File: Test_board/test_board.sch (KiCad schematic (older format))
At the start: 29 parts, among them J1 CONN_01X03_MALE, J2 CONN_02X20, J3 CONN_01X06, J4 CONN_02X20, J5 USB_A, J8 DB9_FEMALE, U1 MAX16056

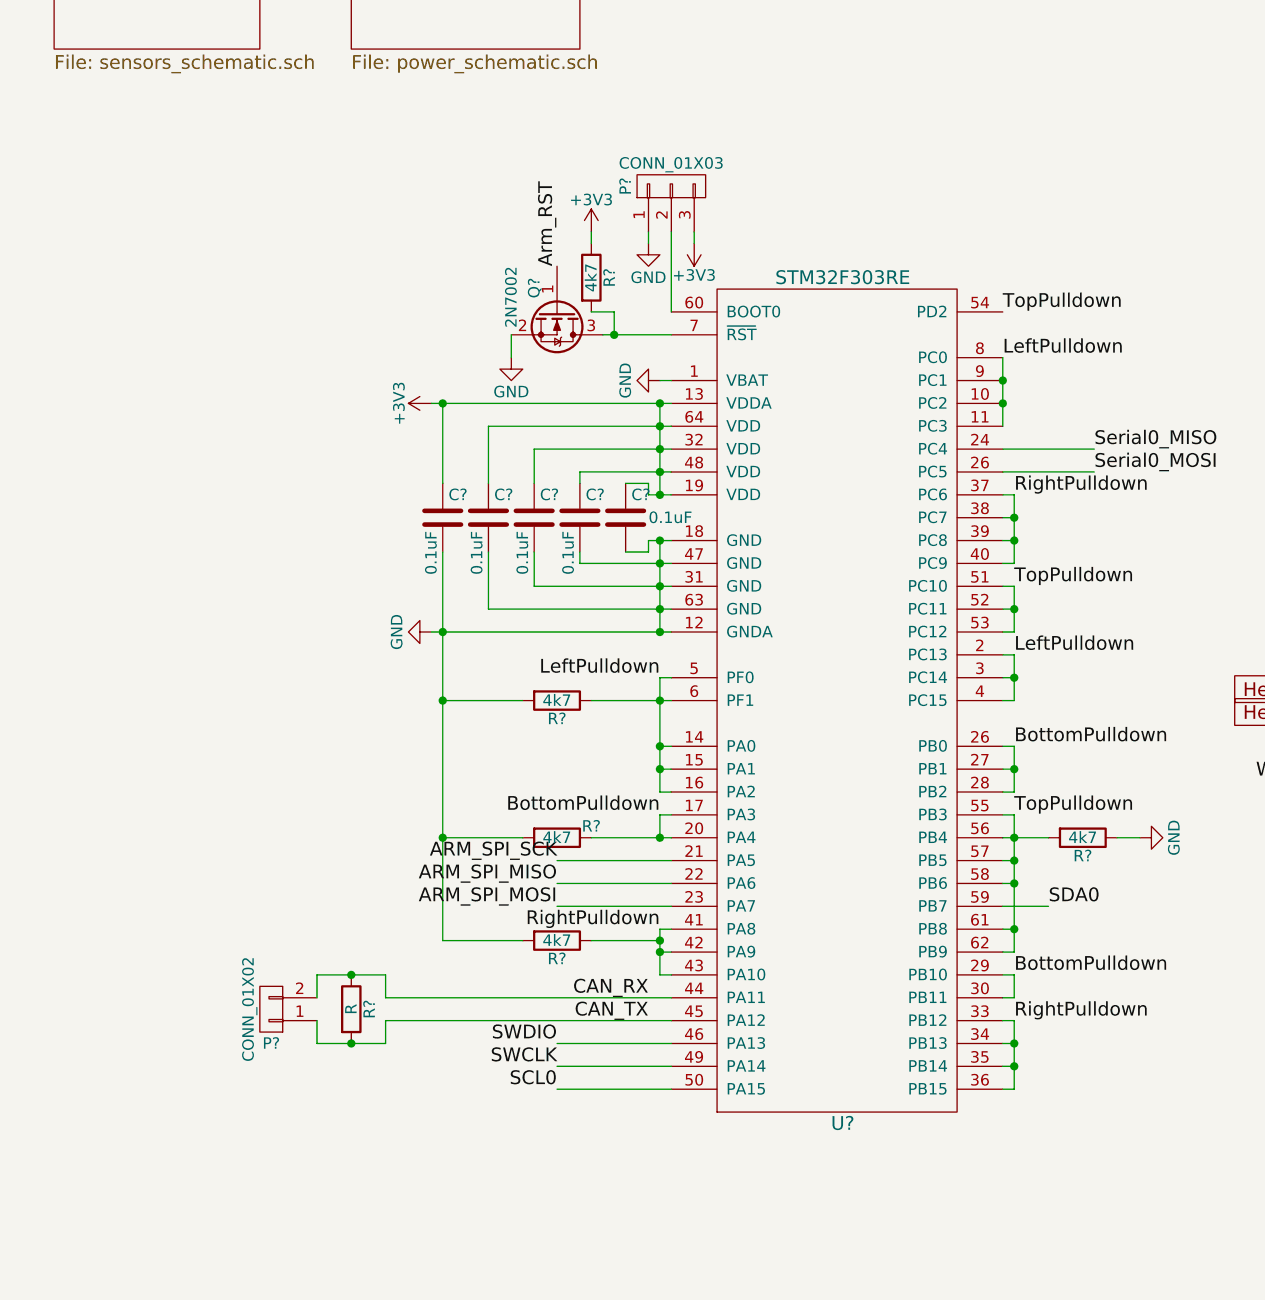
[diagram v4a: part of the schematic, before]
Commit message: Added programming header to diagram. Changed drafting template
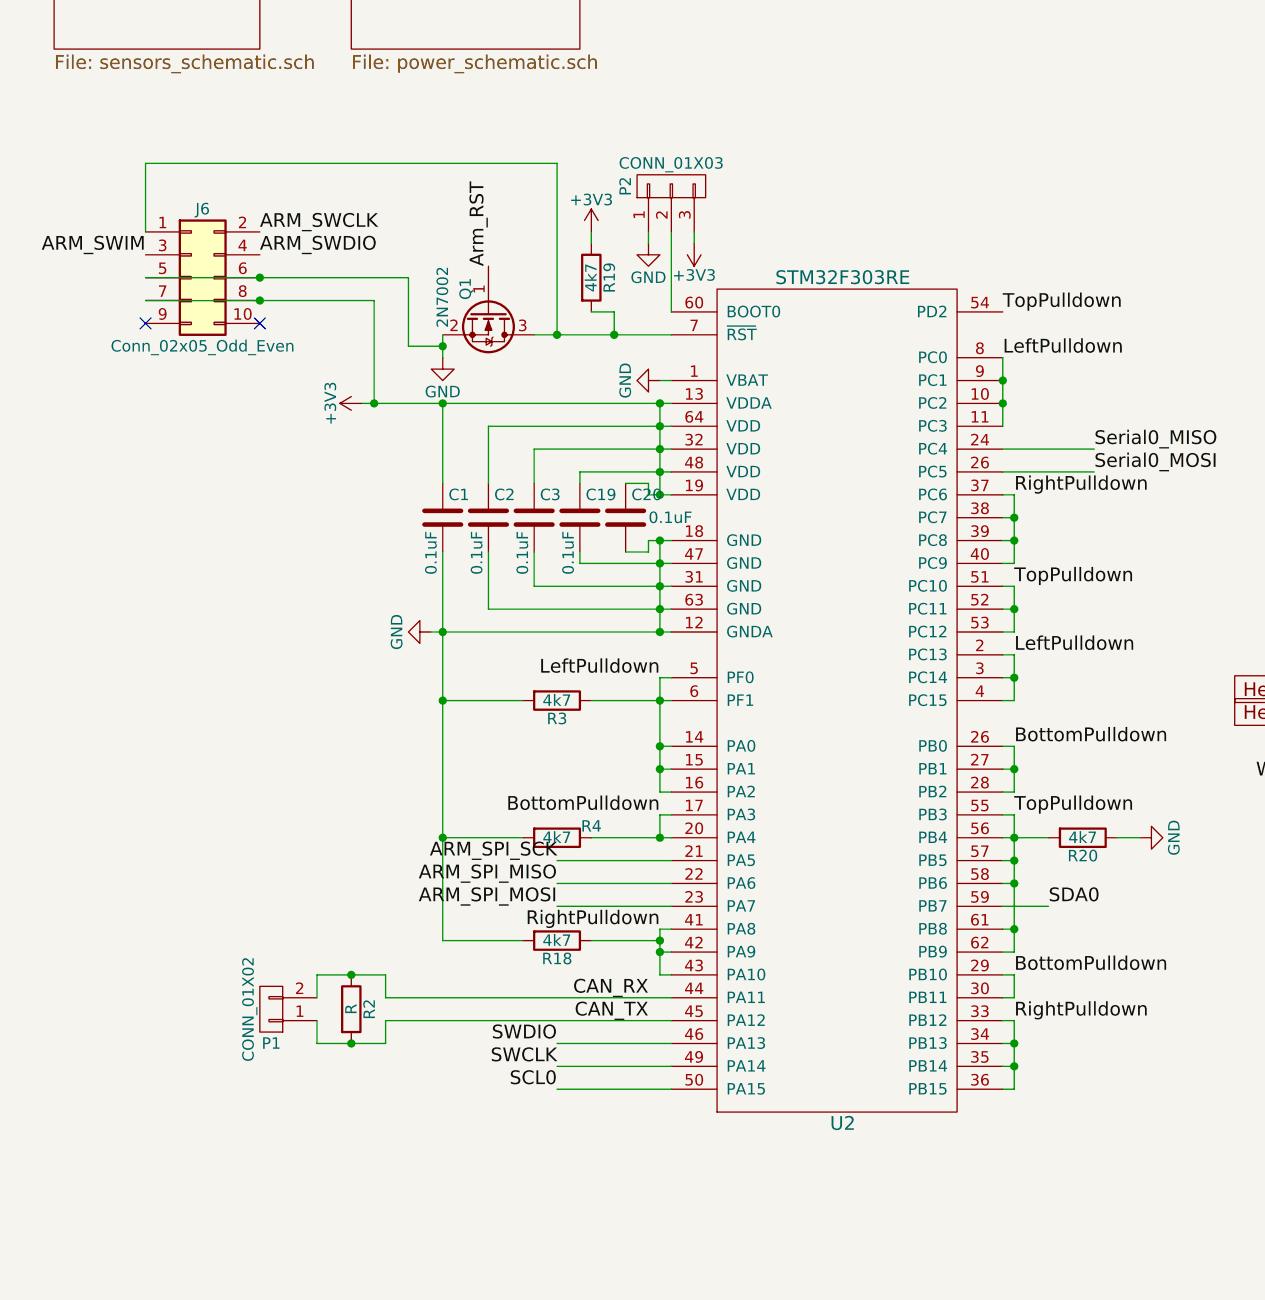
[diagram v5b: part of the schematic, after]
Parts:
- added J6: Conn_02x05_Odd_Even, symbol Conn_02x05_Odd_Even
- gave numbers to parts that had none: 15
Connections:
- net +3V3: now also J6.7 (Pin_7), J6.8 (Pin_8)
- net GND: now also J6.5 (Pin_5), J6.6 (Pin_6)
- net at Q1.3 (D), R19.2, U2.7 (~RST): now also J6.1 (Pin_1)
- new net ARM_SWCLK: J6.2 (Pin_2)
- new net ARM_SWDIO: J6.4 (Pin_4)
- new net ARM_SWIM: J6.3 (Pin_3)
- no-connect marks 7 -> 9
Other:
- moved on the sheet: Q1

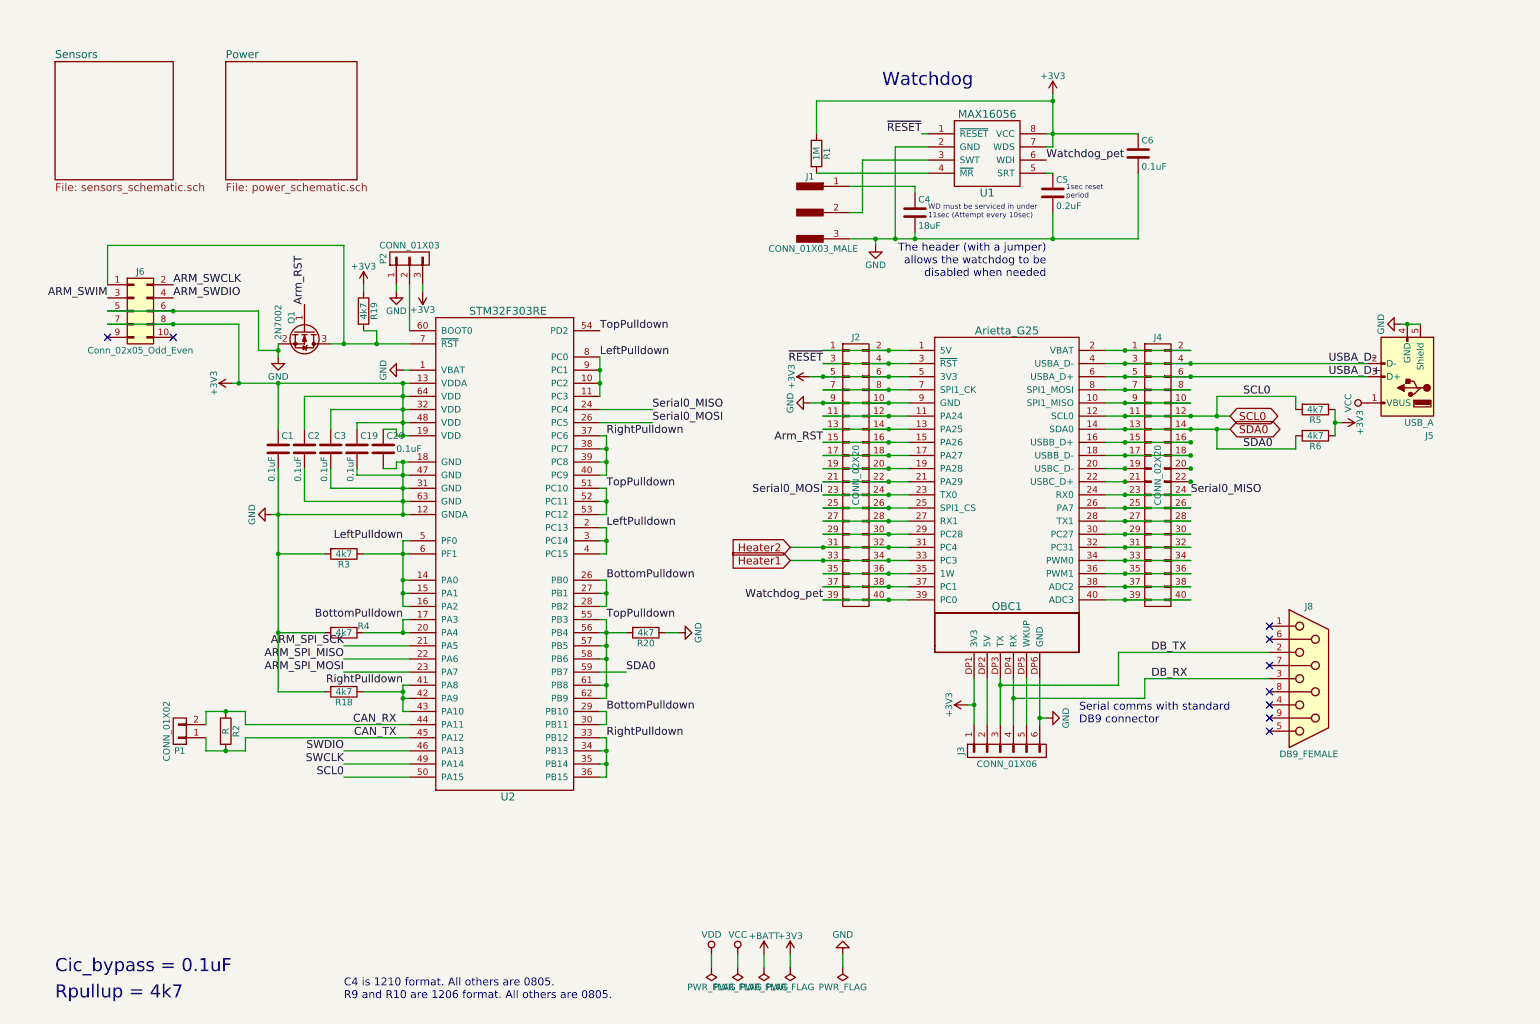
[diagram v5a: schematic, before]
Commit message: Started V2.1, used template, found new programmable buck-boost converter
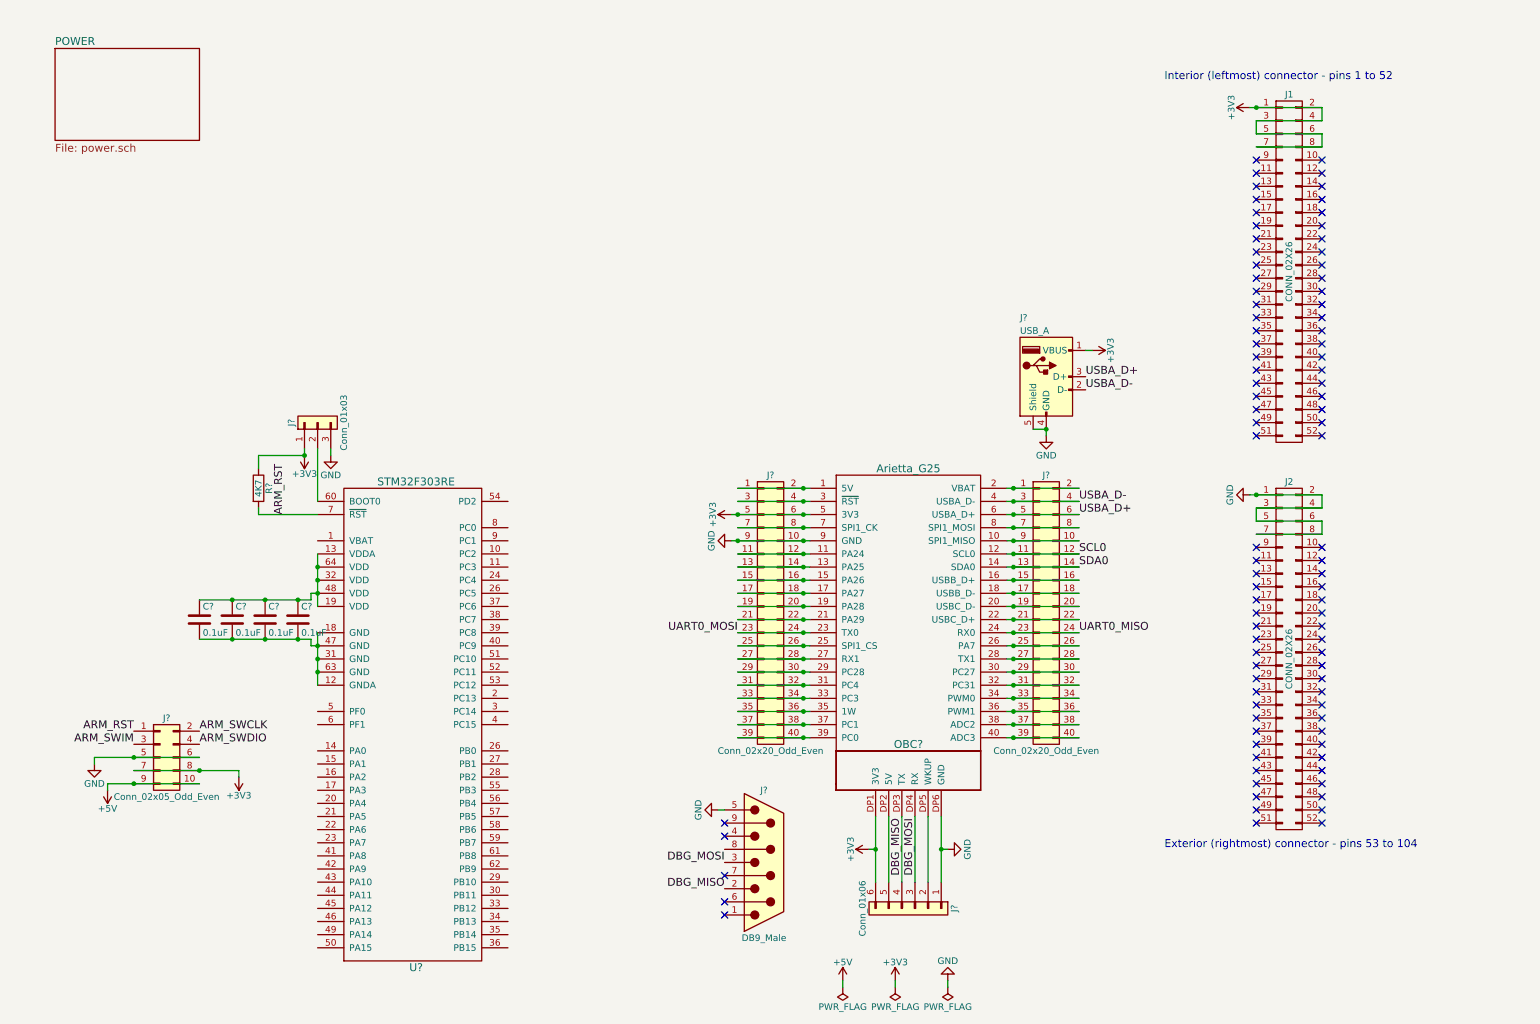
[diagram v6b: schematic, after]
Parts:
- removed C1, C19, C2, C20, C3: 0.1uF, symbol C
- removed C4: 18uF, Capacitors_SMD:C_1210, symbol C
- removed C5: 0.2uF, Capacitors_SMD:C_0805, symbol C
- removed C6: 0.1uF, Capacitors_SMD:C_0805, symbol C
- removed J1: CONN_01X03_MALE, Pin_Headers:Pin_Header_Straight_1x03_Pitch2.54mm, symbol CONN_01X03_MALE
- removed J2, J4: CONN_02X20, Pin_Headers:Pin_Header_Straight_2x20_Pitch2.54mm, symbol CONN_02X20
- removed J3: CONN_01X06, Pin_Headers:Pin_Header_Straight_1x06_Pitch2.54mm, symbol CONN_01X06
- removed J5: USB_A, aleksandr_footprints:USB_A_Board, symbol USB_A-RESCUE-test_board
- removed J6: Conn_02x05_Odd_Even, symbol Conn_02x05_Odd_Even
- removed J8: DB9_FEMALE, Connect:DB9FC, symbol DB9_FEMALE
- removed OBC1: Arietta_G25, aleksandr_footprints:Arietta_G25, symbol Arietta_G25
- removed P1: CONN_01X02, symbol CONN_01X02
- removed P2: CONN_01X03, symbol CONN_01X03
- removed Q1: 2N7002, symbol Q_NMOS_GSD
- removed R1: 1M, Resistors_SMD:R_0805, symbol R
- removed R18, R19, R20, R3, R4: 4k7, symbol R
- removed R2: R, symbol R
- removed R5, R6: 4k7, Resistors_SMD:R_0805, symbol R
- removed U1: MAX16056, Housings_DFN_QFN:DFN-8-1EP_3x3mm_Pitch0.65mm, symbol MAX16056
- removed U2: STM32F303RE, symbol STM32F303RE
- added C? (x4): 0.1uF, 0805, symbol C
- added J1, J2: CONN_02X26, Pin_Headers:Pin_Header_Straight_2x26_Pitch2.54mm, symbol CONN_02X26
- added J? (x2): Conn_02x20_Odd_Even, symbol Conn_02x20_Odd_Even
- added J?: Conn_01x06, symbol Conn_01x06
- added J?: USB_A, symbol USB_A
- added J?: DB9_Male, symbol DB9_Male
- added J?: Conn_02x05_Odd_Even, symbol Conn_02x05_Odd_Even
- added J?: Conn_01x03, symbol Conn_01x03
- added OBC?: Arietta_G25, symbol Arietta_G25
- added R?: 4K7, 0805, symbol R
- added U?: STM32F303RE, symbol STM32F303RE
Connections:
- net +3V3: now also J1.1 (P1), J1.2 (P2), J1.3 (P3), J1.4 (P4), J1.5 (P5), J1.6 (P6), J1.7 (P7), J1.8 (P8), J?.1 (Pin_1), J?.1 (VBUS), J?.5 (Pin_5), J?.6 (Pin_6), J?.6 (Pin_6), J?.7 (Pin_7), J?.8 (Pin_8), OBC?.5 (3V3), OBC?.DP1 (3V3), R?.1
- net ARM_SWCLK: now also J?.2 (Pin_2)
- net ARM_SWDIO: now also J?.4 (Pin_4)
- net ARM_SWIM: now also J?.3 (Pin_3)
- net GND: now also J2.1 (P1), J2.2 (P2), J2.3 (P3), J2.4 (P4), J2.5 (P5), J2.6 (P6), J2.7 (P7), J2.8 (P8), J?.1 (Pin_1), J?.10 (Pin_10), J?.3 (Pin_3), J?.4 (GND), J?.5, J?.5 (Pin_5), J?.5 (Shield), J?.6 (Pin_6), J?.9 (Pin_9), OBC?.9 (GND), OBC?.DP6 (GND)
- net SCL0: now also J?.11 (Pin_11), J?.12 (Pin_12), OBC?.12 (SCL0)
- net SDA0: now also J?.13 (Pin_13), J?.14 (Pin_14), OBC?.14 (SDA0)
- net USBA_D+: now also J?.3 (D+), J?.5 (Pin_5), J?.6 (Pin_6), OBC?.6 (USBA_D+)
- net USBA_D-: now also J?.2 (D-), J?.3 (Pin_3), J?.4 (Pin_4), OBC?.4 (USBA_D-)
- new net: J?.1 (Pin_1), J?.2 (Pin_2), OBC?.1 (5V)
- new net: J?.10 (Pin_10), J?.9 (Pin_9), OBC?.10 (SPI1_MISO)
- new net: J?.11 (Pin_11), J?.12 (Pin_12), OBC?.11 (PA24)
- new net: J?.13 (Pin_13), J?.14 (Pin_14), OBC?.13 (PA25)
- new net: J?.15 (Pin_15), J?.16 (Pin_16), OBC?.15 (PA26)
- new net: J?.15 (Pin_15), J?.16 (Pin_16), OBC?.16 (USBB_D+)
- new net: J?.17 (Pin_17), J?.18 (Pin_18), OBC?.17 (PA27)
- new net: J?.17 (Pin_17), J?.18 (Pin_18), OBC?.18 (USBB_D-)
- new net: J?.19 (Pin_19), J?.20 (Pin_20), OBC?.19 (PA28)
- new net: J?.1 (Pin_1), J?.2 (Pin_2), OBC?.2 (VBAT)
- new net: J?.19 (Pin_19), J?.20 (Pin_20), OBC?.20 (USBC_D-)
- new net: J?.21 (Pin_21), J?.22 (Pin_22), OBC?.21 (PA29)
- new net: J?.21 (Pin_21), J?.22 (Pin_22), OBC?.22 (USBC_D+)
- new net: J?.25 (Pin_25), J?.26 (Pin_26), OBC?.25 (SPI1_CS)
- new net: J?.25 (Pin_25), J?.26 (Pin_26), OBC?.26 (PA7)
- new net: J?.27 (Pin_27), J?.28 (Pin_28), OBC?.27 (RX1)
- new net: J?.27 (Pin_27), J?.28 (Pin_28), OBC?.28 (TX1)
- new net: J?.29 (Pin_29), J?.30 (Pin_30), OBC?.29 (PC28)
- new net: J?.3 (Pin_3), J?.4 (Pin_4), OBC?.3 (~RST)
- new net: J?.29 (Pin_29), J?.30 (Pin_30), OBC?.30 (PC27)
- new net: J?.31 (Pin_31), J?.32 (Pin_32), OBC?.31 (PC4)
- new net: J?.31 (Pin_31), J?.32 (Pin_32), OBC?.32 (PC31)
- new net: J?.33 (Pin_33), J?.34 (Pin_34), OBC?.33 (PC3)
- new net: J?.33 (Pin_33), J?.34 (Pin_34), OBC?.34 (PWM0)
- new net: J?.35 (Pin_35), J?.36 (Pin_36), OBC?.35 (1W)
- new net: J?.35 (Pin_35), J?.36 (Pin_36), OBC?.36 (PWM1)
- new net: J?.37 (Pin_37), J?.38 (Pin_38), OBC?.37 (PC1)
- new net: J?.37 (Pin_37), J?.38 (Pin_38), OBC?.38 (ADC2)
- new net: J?.39 (Pin_39), J?.40 (Pin_40), OBC?.39 (PC0)
- new net: J?.39 (Pin_39), J?.40 (Pin_40), OBC?.40 (ADC3)
- new net: J?.7 (Pin_7), J?.8 (Pin_8), OBC?.7 (SPI1_CK)
- new net: J?.7 (Pin_7), J?.8 (Pin_8), OBC?.8 (SPI1_MOSI)
- new net: J?.5 (Pin_5), OBC?.DP2 (5V)
- new net: J?.2 (Pin_2), OBC?.DP5 (WKUP)
- new net: C?.2, C?.2, C?.2, C?.2, U?.12 (GNDA), U?.18 (GND), U?.31 (GND), U?.47 (GND), U?.63 (GND)
- new net: C?.1, C?.1, C?.1, C?.1, U?.13 (VDDA), U?.19 (VDD), U?.32 (VDD), U?.48 (VDD), U?.64 (VDD)
- new net: J?.2 (Pin_2), U?.60 (BOOT0)
- new net +5V: J?.10 (Pin_10), J?.9 (Pin_9)
- new net ARM_RST: J?.1 (Pin_1), R?.2, U?.7 (~RST)
- new net DBG_MISO: J?.2, J?.4 (Pin_4), OBC?.DP3 (TX)
- new net DBG_MOSI: J?.3, J?.3 (Pin_3), OBC?.DP4 (RX)
- new net UART0_MISO: J?.23 (Pin_23), J?.24 (Pin_24), OBC?.24 (RX0)
- new net UART0_MOSI: J?.23 (Pin_23), J?.24 (Pin_24), OBC?.23 (TX0)
- no-connect marks 9 -> 93
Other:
- note added: "Exterior (rightmost) connector - pins 53 to 104"
- note added: "Interior (leftmost) connector - pins 1 to 52"
- note removed: "1sec reset\nperiod"
- note removed: "C4 is 1210 format. All others are 0805.\nR9 and R10 are 1206 format. All others are 0805.\n"
- note removed: "Cic_bypass = 0.1uF"
- note removed: "Rpullup = 4k7"
- note removed: "Serial comms with standard \nDB9 connector\n"
- note removed: "The header (with a jumper)\nallows the watchdog to be\ndisabled when needed"
- note removed: "WD must be serviced in under \n11sec (Attempt every 10sec)"
- note removed: "Watchdog\n"
